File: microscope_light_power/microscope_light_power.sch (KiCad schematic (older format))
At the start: 30 parts

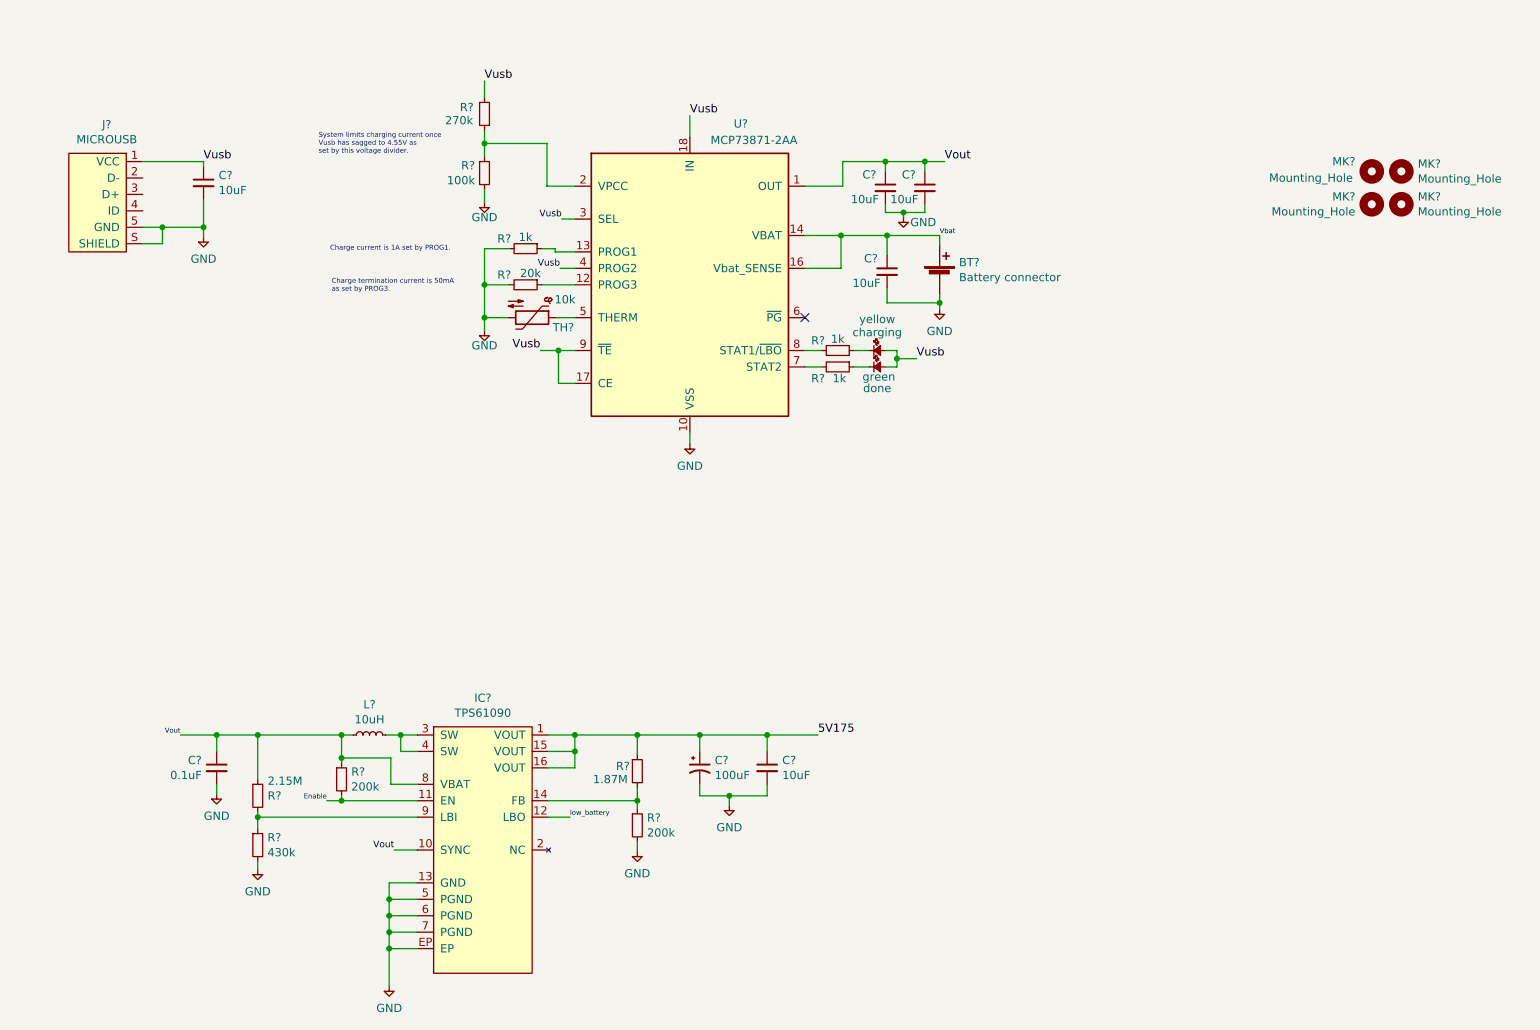
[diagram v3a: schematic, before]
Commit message: Added power out connector and enable switch connector. A handful of test points were also added (I finally remembered to do this before sending a board out!!!!)
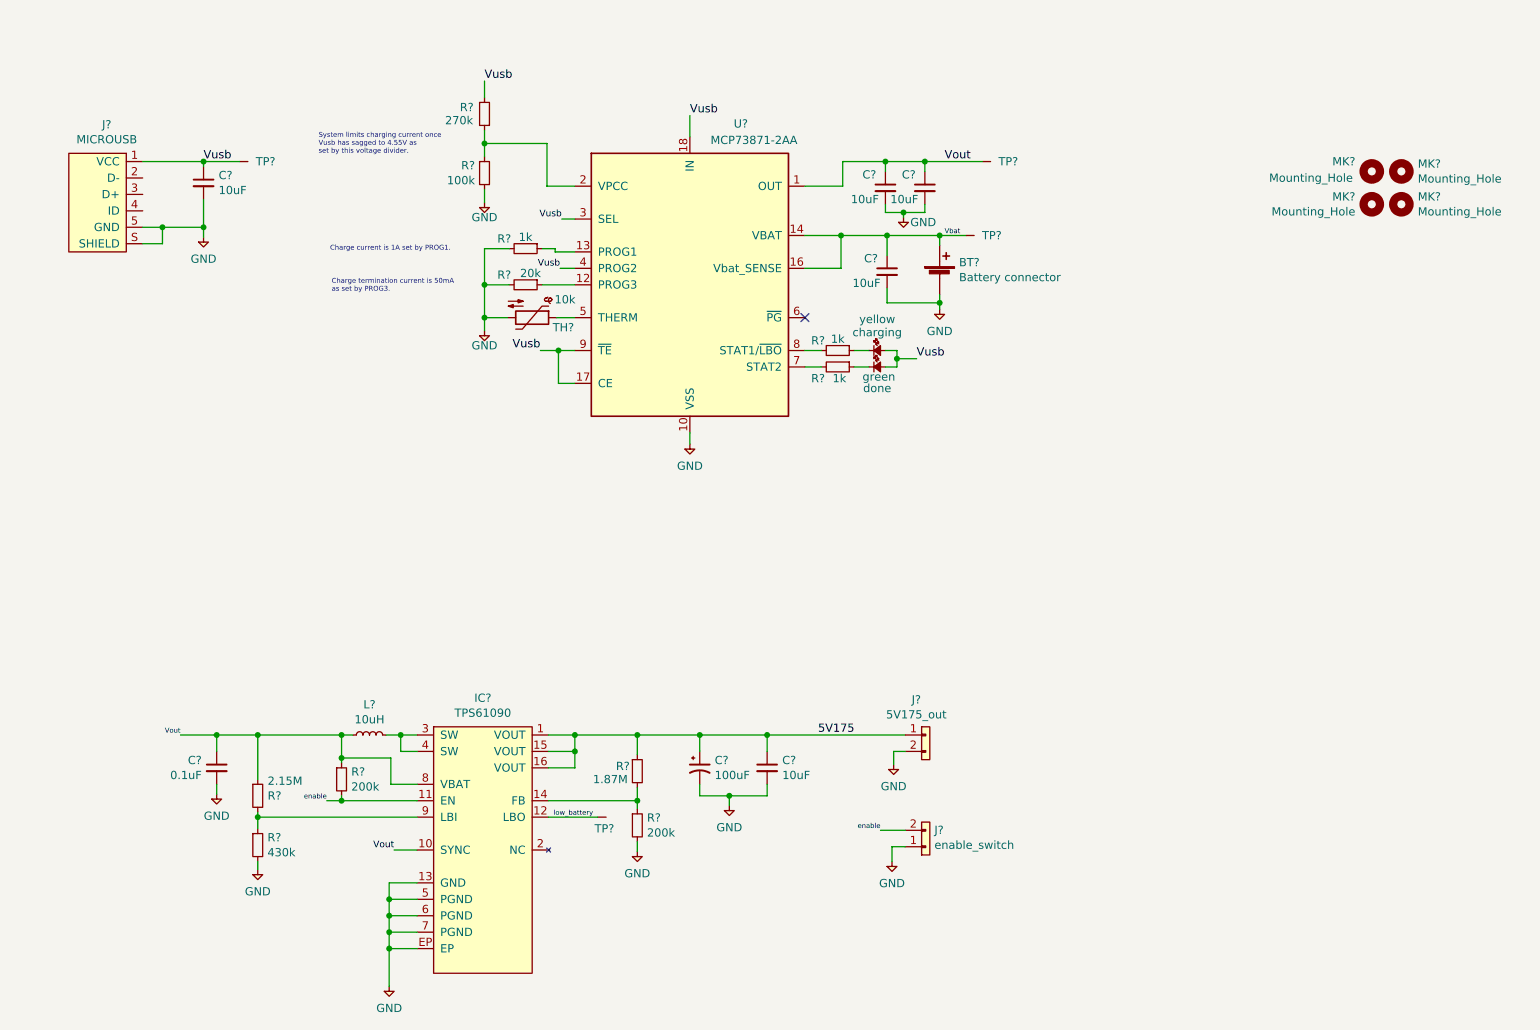
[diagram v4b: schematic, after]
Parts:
- added J?: enable_switch, Connectors_JST:JST_PH_S2B-PH-K_02x2.00mm_Angled, symbol CONN_01x02
- added J?: 5V175_out, Connectors_JST:JST_PH_S2B-PH-K_02x2.00mm_Angled, symbol CONN_01x02
- added TP?: TESTPAD, Measurement_Points:Measurement_Point_Round-TH_Small, symbol TESTPAD
- added TP? (x3): TESTPAD, agg:TESTPAD, symbol TESTPAD
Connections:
- net 5V175: now also J?.1
- net GND: now also J?.1, J?.2
- net Vbat: now also TP?.1 (TP)
- net Vout: now also TP?.1 (TP)
- net Vusb: now also TP?.1 (TP)
- net low_battery: now also TP?.1 (TP)
- net Enable renamed enable
- net enable: now also J?.2
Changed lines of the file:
@@
 	0    -1   -1   0
 $EndComp
-Text Label 6480 1860 0    30   ~ 0
+Text Label 6510 1860 0    30   ~ 0
 Vbat
 Text Label 3160 5600 2    40   ~ 0
@@
 $EndComp
 Text Label 2750 5300 2    30   ~ 0
-Enable
+enable
 $Comp
 L GND #PWR?
@@
 	1    0    0    -1
 $EndComp
-Text Label 4230 5400 0    30   ~ 0
+Text Label 4130 5400 0    30   ~ 0
 low_battery
 $Comp
@@
 $EndComp
 Wire Wire Line
-	1630 1410 2000 1410
+	1630 1410 2220 1410
 Wire Wire Line
 	2000 1410 2000 1440
@@
 	4260 1760 4180 1760
 Wire Wire Line
-	5660 1860 6480 1860
+	5660 1860 6640 1860
 Wire Wire Line
 	6480 1860 6480 1920
@@
 	6390 1410 6390 1470
 Wire Wire Line
-	5890 1410 6510 1410
+	5890 1410 6740 1410
 Wire Wire Line
 	6150 1410 6150 1470
@@
 	2330 5670 2330 5720
 Wire Wire Line
-	4100 5400 4230 5400
-Wire Wire Line
-	4100 4900 5740 4900
+	4100 5400 4400 5400
+Wire Wire Line
+	4100 4900 6270 4900
 Wire Wire Line
 	4100 5000 4260 5000
@@
 	0    1    1    0
 $EndComp
+$Comp
+L CONN_01x02 J?
+U 1 1 59FBD39A
+P 6370 5580
+F 0 "J?" H 6292 5479 50  0000 R CNN
+F 1 "enable_switch" H 6292 5570 50  0000 R CNN
+F 2 "Connectors_JST:JST_PH_S2B-PH-K_02x2.00mm_Angled" H 6370 5580 50  0001 C CNN
+F 3 "" H 6370 5580 50  0001 C CNN
+	1    6370 5580
+	-1   0    0    1
+$EndComp
+$Comp
+L CONN_01x02 J?
+U 1 1 59FBD6E0
+P 6370 4900
+F 0 "J?" H 6402 5115 50  0000 C CNN
+F 1 "5V175_out" H 6402 5024 50  0000 C CNN
+F 2 "Connectors_JST:JST_PH_S2B-PH-K_02x2.00mm_Angled" H 6370 4900 50  0001 C CNN
+F 3 "" H 6370 4900 50  0001 C CNN
+	1    6370 4900
+	-1   0    0    -1
+$EndComp
+$Comp
+L GND #PWR?
+U 1 1 59FC5FD9
+P 6200 5080
+F 0 "#PWR?" H 6070 5120 50  0001 L CNN
+F 1 "GND" H 6200 4947 50  0000 C CNN
+F 2 "" H 6200 5080 50  0001 C CNN
+F 3 "" H 6200 5080 50  0001 C CNN
+	1    6200 5080
+	1    0    0    -1
+$EndComp
+Wire Wire Line
+	6270 5000 6200 5000
+Wire Wire Line
+	6200 5000 6200 5080
+Text Label 6120 5480 2    30   ~ 0
+enable
+$Comp
+L GND #PWR?
+U 1 1 59FCBF9F
+P 6190 5670
+F 0 "#PWR?" H 6060 5710 50  0001 L CNN
+F 1 "GND" H 6190 5537 50  0000 C CNN
+F 2 "" H 6190 5670 50  0001 C CNN
+F 3 "" H 6190 5670 50  0001 C CNN
+	1    6190 5670
+	1    0    0    -1
+$EndComp
+Wire Wire Line
+	6190 5670 6190 5580
+Wire Wire Line
+	6190 5580 6270 5580
+Wire Wire Line
+	6270 5480 6120 5480
+$Comp
+L TESTPAD TP?
+U 1 1 59FD2D5E
+P 4400 5400
+F 0 "TP?" H 4380 5330 50  0000 L CNN
+F 1 "TESTPAD" H 4400 5325 50  0001 L CNN
+F 2 "Measurement_Points:Measurement_Point_Round-TH_Small" H 4400 5250 50  0001 L CNN
+F 3 "" H 4400 5400 50  0001 C CNN
+	1    4400 5400
+	1    0    0    -1
+$EndComp
+$Comp
+L TESTPAD TP?
+U 1 1 59FD7F8A
+P 6740 1410
+F 0 "TP?" H 6838 1410 50  0000 L CNN
+F 1 "TESTPAD" H 6740 1335 50  0001 L CNN
+F 2 "agg:TESTPAD" H 6740 1260 50  0001 L CNN
+F 3 "" H 6740 1410 50  0001 C CNN
+	1    6740 1410
+	1    0    0    -1
+$EndComp
+$Comp
+L TESTPAD TP?
+U 1 1 59FD88E1
+P 2220 1410
+F 0 "TP?" H 2318 1410 50  0000 L CNN
+F 1 "TESTPAD" H 2220 1335 50  0001 L CNN
+F 2 "agg:TESTPAD" H 2220 1260 50  0001 L CNN
+F 3 "" H 2220 1410 50  0001 C CNN
+	1    2220 1410
+	1    0    0    -1
+$EndComp
+Connection ~ 2000 1410
+$Comp
+L TESTPAD TP?
+U 1 1 59FDA6BA
+P 6640 1860
+F 0 "TP?" H 6738 1860 50  0000 L CNN
+F 1 "TESTPAD" H 6640 1785 50  0001 L CNN
+F 2 "agg:TESTPAD" H 6640 1710 50  0001 L CNN
+F 3 "" H 6640 1860 50  0001 C CNN
+	1    6640 1860
+	1    0    0    -1
+$EndComp
+Connection ~ 6480 1860
 $EndSCHEMATC

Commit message: Update agg-kicad library.
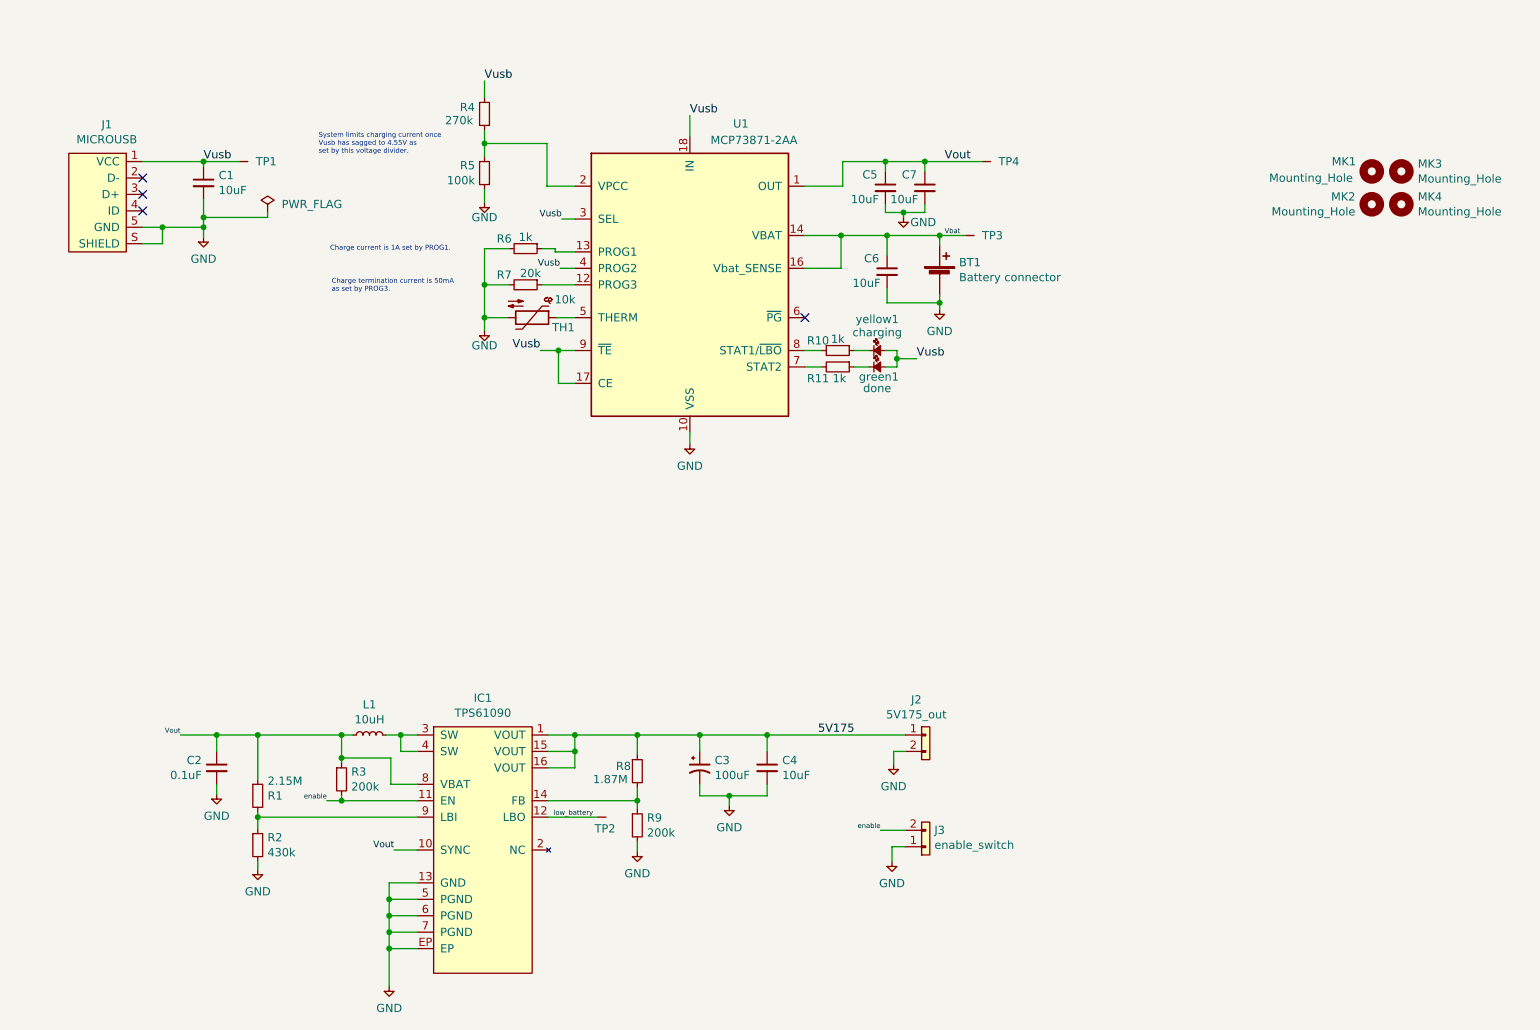
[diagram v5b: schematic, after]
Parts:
- gave numbers to parts that had none: 34
- renumbered green to green1, yellow to yellow1
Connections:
- no-connect marks 1 -> 4

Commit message: Select footprint for the last part (10uH inductor). Ready to move on to laying out the PCB!
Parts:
- L1: footprint (none) -> Inductors:Inductor_Taiyo-Yuden_NR-80xx_HandSoldering
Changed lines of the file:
@@
 F 0 "L1" V 3195 4900 50  0000 C CNN
 F 1 "10uH" V 3104 4900 50  0000 C CNN
-F 2 "" H 3010 4900 50  0001 C CNN
+F 2 "Inductors:Inductor_Taiyo-Yuden_NR-80xx_HandSoldering" H 3010 4900 50  0001 C CNN
 F 3 "" H 3010 4900 50  0001 C CNN
 F 4 "NR8040T100M" V 3010 4900 60  0001 C CNN "part number"

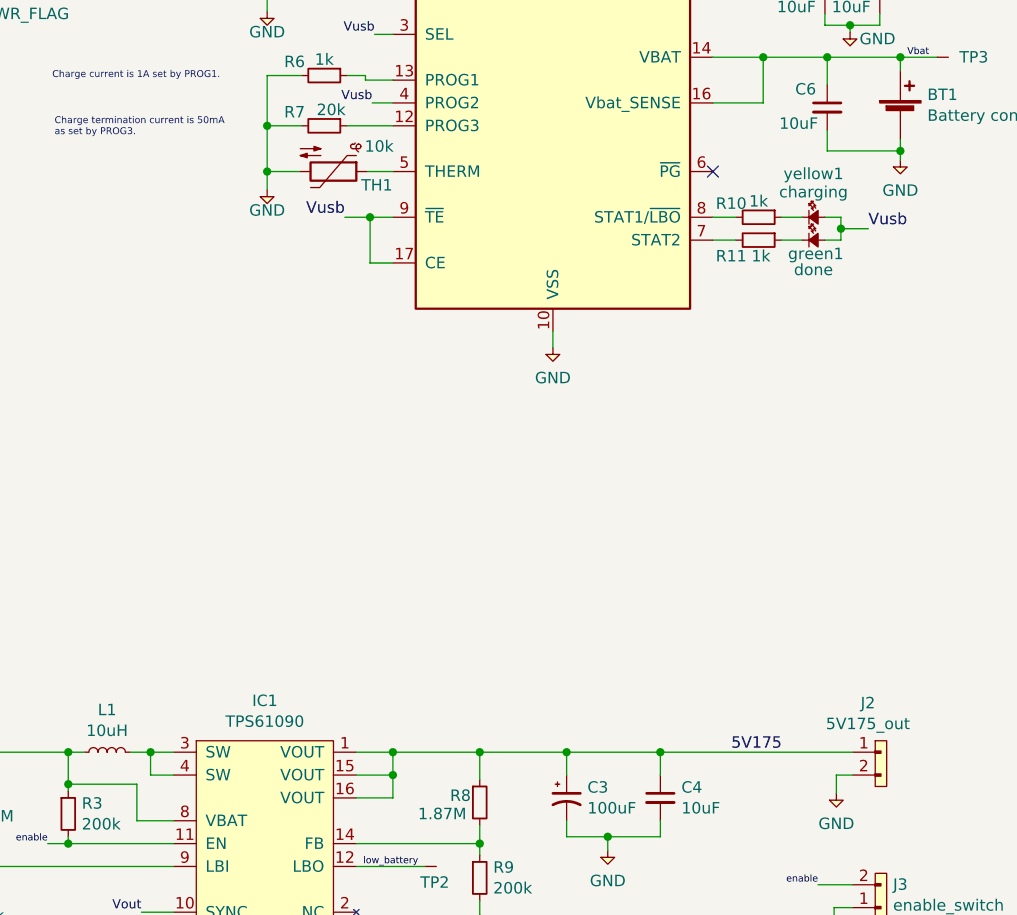
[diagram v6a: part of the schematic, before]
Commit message: Put the parts for the MCP73871 battery charger in better locations. Some labeling was also placed to make sure the board can be used without looking at the schematic every time!
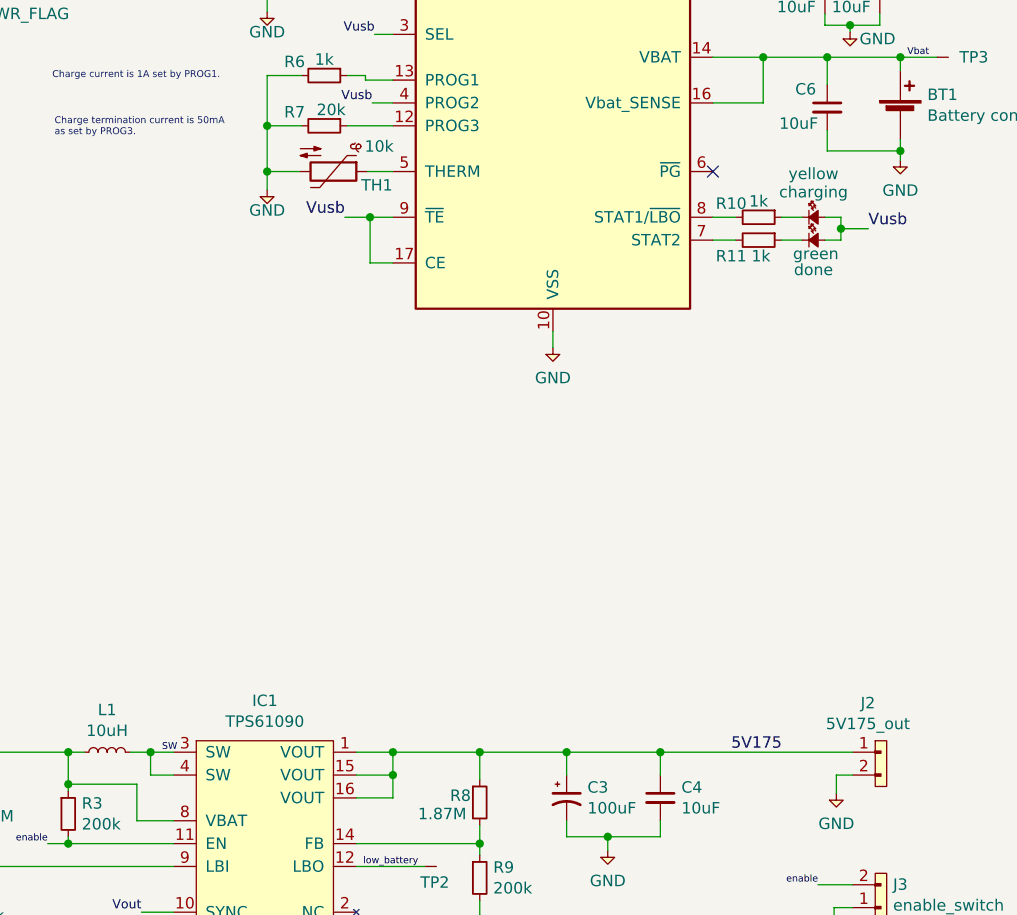
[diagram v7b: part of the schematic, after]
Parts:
- renumbered green1 to green, yellow1 to yellow
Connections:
- net SW: now reaches IC1.3 (SW), IC1.4 (SW), L1.2
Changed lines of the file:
@@
 Vusb
 $Comp
-L LED yellow1
+L LED yellow
 U 1 1 59DA5C71
 P 6050 2560
-F 0 "yellow1" H 6100 2750 50  0000 C CNN
+F 0 "yellow" H 6100 2750 50  0000 C CNN
 F 1 "charging" H 6100 2670 50  0000 C CNN
 F 2 "LEDs:LED_0603_HandSoldering" H 6050 2560 50  0001 C CNN
@@
 $EndComp
 $Comp
-L LED green1
+L LED green
 U 1 1 59DA7F2A
 P 6050 2660
-F 0 "green1" H 6110 2600 50  0000 C CNN
+F 0 "green" H 6110 2600 50  0000 C CNN
 F 1 "done" H 6100 2530 50  0000 C CNN
 F 2 "LEDs:LED_0603_HandSoldering" H 6050 2660 50  0001 C CNN
@@
 Wire Wire Line
 	2390 1750 2390 1720
+Text Label 3250 4900 0    30   ~ 0
+SW
 $EndSCHEMATC

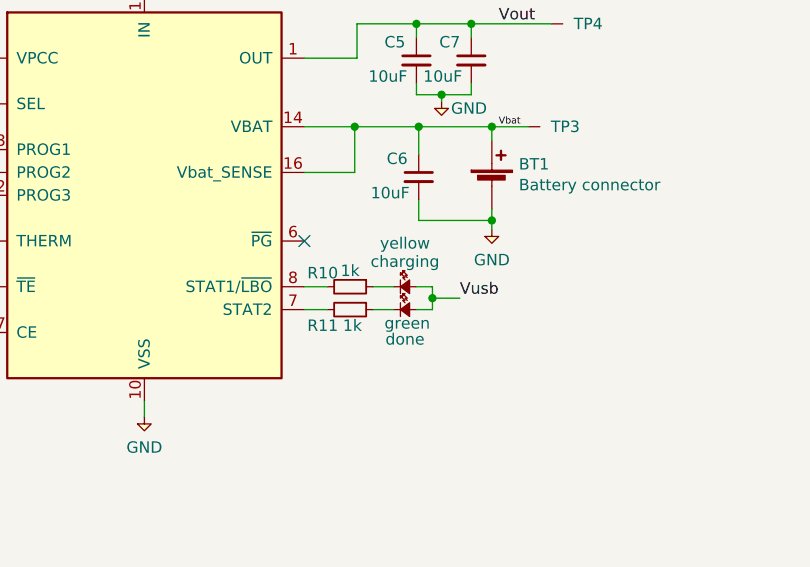
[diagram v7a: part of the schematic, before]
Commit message: Route the most critical power traces.
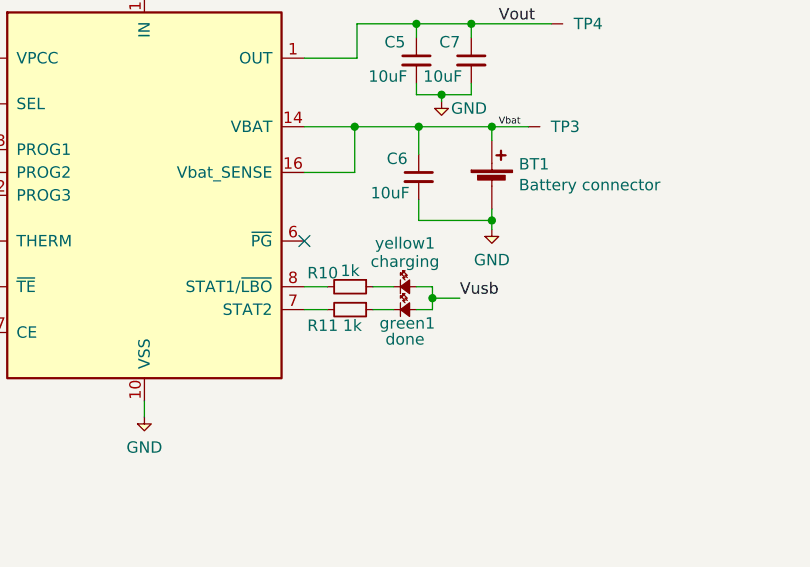
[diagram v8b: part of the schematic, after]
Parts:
- renumbered green to green1, yellow to yellow1
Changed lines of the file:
@@
 Vusb
 $Comp
-L LED yellow
+L LED yellow1
 U 1 1 59DA5C71
 P 6050 2560
-F 0 "yellow" H 6100 2750 50  0000 C CNN
+F 0 "yellow1" H 6100 2750 50  0000 C CNN
 F 1 "charging" H 6100 2670 50  0000 C CNN
 F 2 "LEDs:LED_0603_HandSoldering" H 6050 2560 50  0001 C CNN
@@
 $EndComp
 $Comp
-L LED green
+L LED green1
 U 1 1 59DA7F2A
 P 6050 2660
-F 0 "green" H 6110 2600 50  0000 C CNN
+F 0 "green1" H 6110 2600 50  0000 C CNN
 F 1 "done" H 6100 2530 50  0000 C CNN
 F 2 "LEDs:LED_0603_HandSoldering" H 6050 2660 50  0001 C CNN
